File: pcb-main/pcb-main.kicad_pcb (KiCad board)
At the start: 2 copper layers, 86 x 86 mm, 37 parts, among them J1 AVR-ISP-6, J2 Conn_02x06_Counter_Clockwise, M1 Stepper_Motor, SW1 SW_MEC_5E, SW2 SW_MEC_5E, U1 ATmega328P-AU, U2 HT1621B-LQFP-A, U3 VIM878, U4 PCF8563T, Y1 16MHz, Y2 32kHz

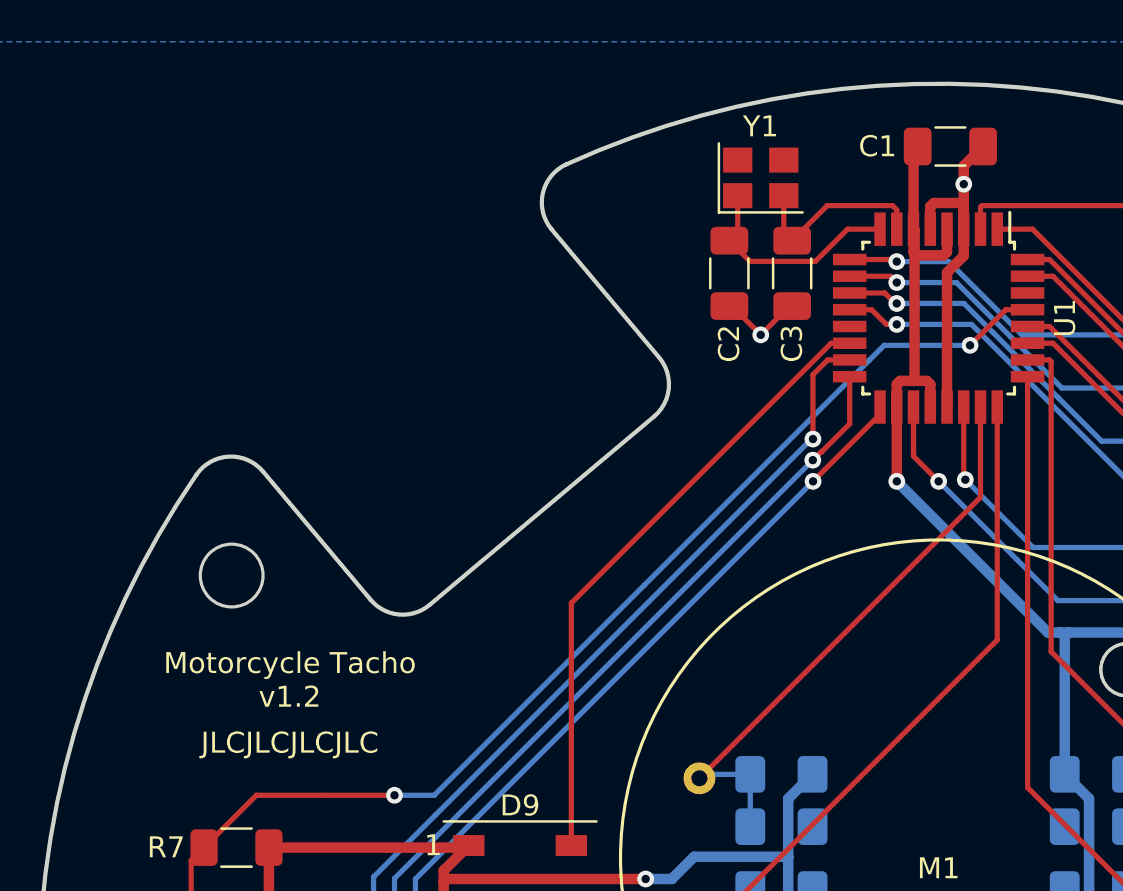
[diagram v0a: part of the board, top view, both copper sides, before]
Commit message: resolves #52: crystal circuit
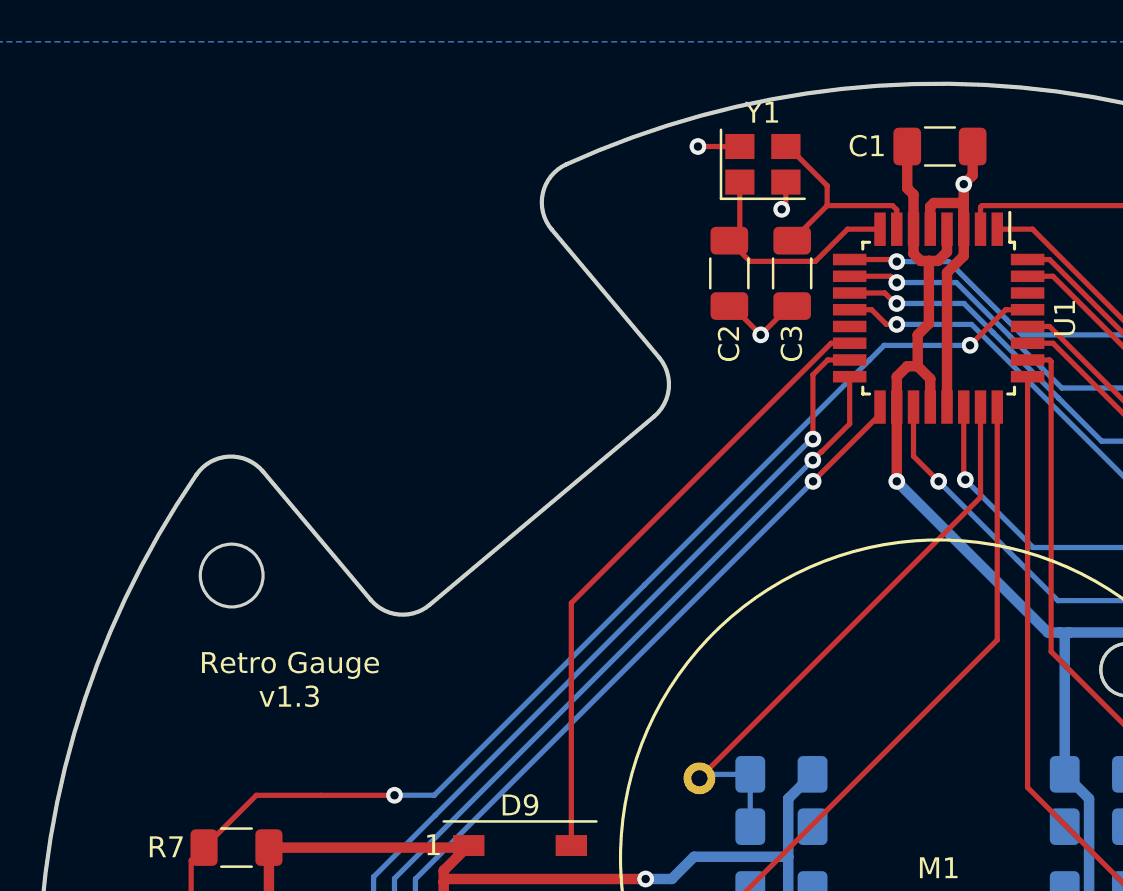
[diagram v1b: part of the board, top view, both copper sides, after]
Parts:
- R1: value 10k -> 100k
- Y1: value 16MHz -> Crystal_GND24
- moved Y1 0.66 mm to (141.6, 60.9)
- moved C1 0.50 mm to (150.1, 60.0)
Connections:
- Y1 pad 2: /XTAL1 -> GND
- Y1 pad 3: (no net) -> /XTAL1
- Y1 pad 4: (no net) -> GND
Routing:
- net GND: track 104.9 -> 108.0 mm, vias 10 -> 12
- net /XTAL1: track 9.02 -> 11.0 mm
- net +5V: track 263.5 -> 262.7 mm
- net /XTAL2: track 10.6 -> 11.3 mm
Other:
- board text added: "Retro Gauge v1.3"
- board text removed: "JLCJLCJLCJLC"
- board text removed: "Motorcycle Tacho v1.2"

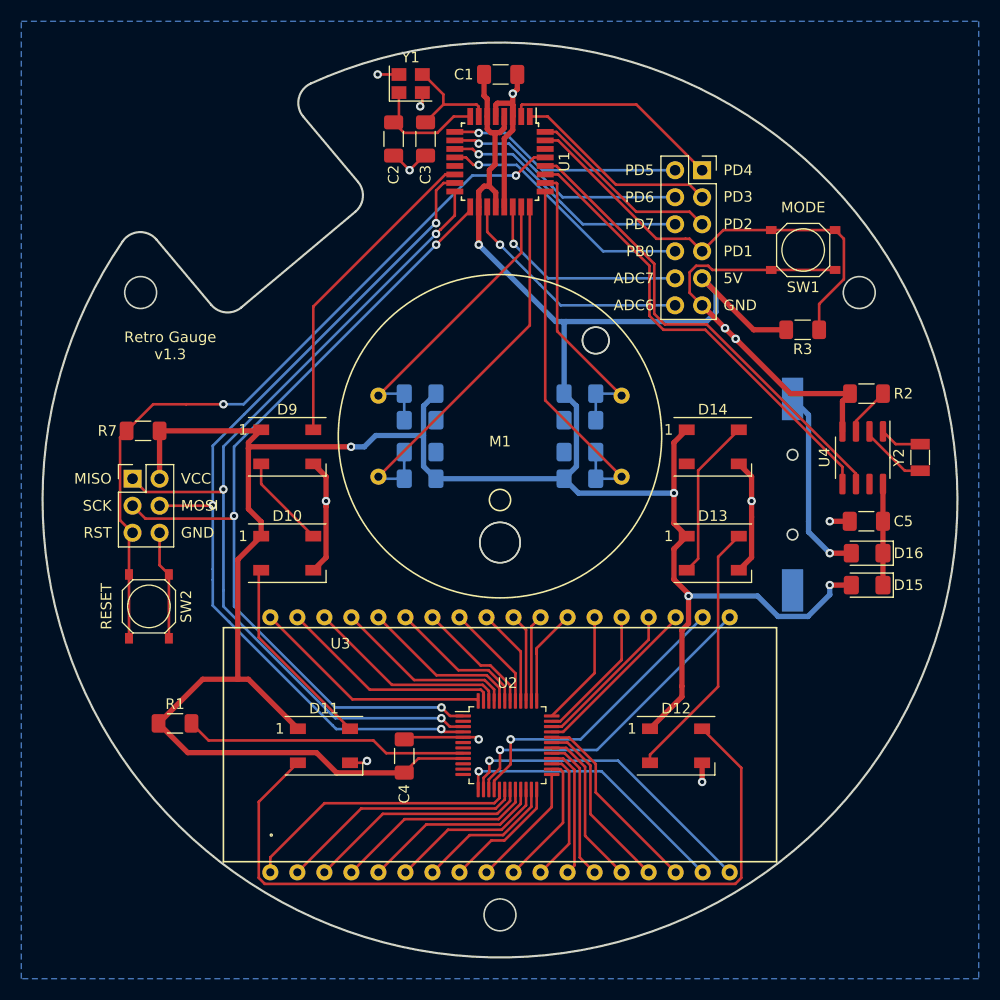
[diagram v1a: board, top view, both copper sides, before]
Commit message: resolves #48: neopixel caps
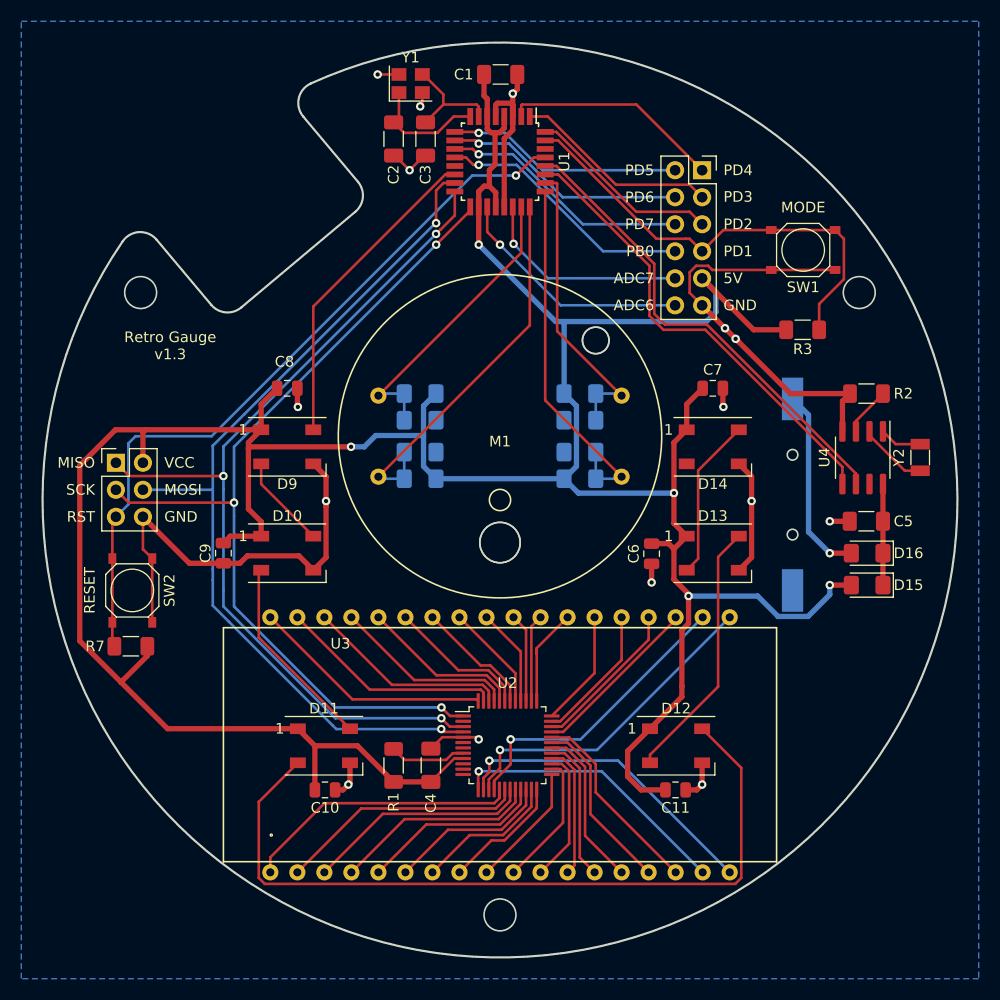
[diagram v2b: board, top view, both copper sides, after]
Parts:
- added C10: 100n, Capacitor_SMD:C_0805_2012Metric, F.Cu at (133.6, 127.2)
- added C11: 100n, Capacitor_SMD:C_0805_2012Metric, F.Cu at (166.5, 127.2)
- added C6: 100n, Capacitor_SMD:C_0805_2012Metric, F.Cu at (164.2, 105.0)
- added C7: 100n, Capacitor_SMD:C_0805_2012Metric, F.Cu at (170.0, 89.5)
- added C8: 100n, Capacitor_SMD:C_0805_2012Metric, F.Cu at (130.0, 89.5)
- added C9: 100n, Capacitor_SMD:C_0805_2012Metric, F.Cu at (124.0, 105.0)
- moved R1 20.9 mm to (140.0, 125.0), turned to 90 degrees
- moved R7 20.3 mm to (115.3, 113.8)
- moved C4 2.65 mm to (143.5, 124.9)
- moved J1 2.17 mm to (113.9, 96.5)
- moved SW2 2.17 mm to (115.4, 108.5)
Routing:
- net +5V: track 262.7 -> 300.1 mm
- net GND: track 108.0 -> 133.8 mm, vias 12 -> 15
- net Net-(R1-Pad2): track 26.7 -> 7.23 mm
- net /PB3: track 83.3 -> 84.8 mm, vias 3 -> 2
- net /PB4: track 84.4 -> 85.9 mm
- net /PB5: track 82.7 -> 84.2 mm
- net /XTAL1: track 11.0 -> 10.4 mm
- net /RESET: track 70.4 -> 70.1 mm, vias 2 -> 1

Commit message: pcb cleanup
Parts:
- moved R3 2.79 mm to (178.0, 81.2), turned to 0 degrees
- moved SW1 0.90 mm to (178.0, 75.8), turned to 90 degrees
- moved R7 0.20 mm to (115.5, 113.8)
- moved SW2 0.06 mm to (115.5, 108.5)
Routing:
- net GND: track 133.8 -> 119.2 mm, vias 15 -> 14
- net /PD1: track 43.1 -> 34.8 mm
- net /RESET: track 70.1 -> 66.8 mm
- net +5V: track 300.1 -> 297.9 mm, vias 5 -> 6

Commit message: update layout
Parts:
- removed SW2: SW_MEC_5E, footprints:TS_1187A
- added J3: Conn_01x02_Male, Connector_JST:JST_PH_S2B-PH-K_1x02_P2.00mm_Horizontal, F.Cu at (175.8, 77.8)
- C1, C2, C3, C4, C5: footprint Capacitor_SMD:C_1206_3216Metric_Pad1.33x1.80mm_HandSolder -> Capacitor_SMD:C_0805_2012Metric
- D15, D16: footprint Diode_SMD:D_1206_3216Metric_Pad1.42x1.75mm_HandSolder -> Diode_SMD:D_0805_2012Metric
- J2: footprint Connector_PinSocket_2.54mm:PinSocket_2x06_P2.54mm_Vertical -> Connector_PinHeader_2.00mm:PinHeader_2x06_P2.00mm_Vertical; moved to B.Cu
- R1, R2, R3, R7: footprint Resistor_SMD:R_1206_3216Metric_Pad1.30x1.75mm_HandSolder -> Resistor_SMD:R_0805_2012Metric
- SW1: value SW_MEC_5E -> SW_Push; footprint footprints:TS_1187A -> Button_Switch_SMD:SW_SPST_TL3342
- moved SW1 70.6 mm to (115.3, 108.3)
- moved J2 7.65 mm to (164.2, 63.0), turned to 180 degrees
- moved C5 7.34 mm to (189.0, 96.2), turned to 90 degrees
- moved Y2 6.95 mm to (186.0, 90.0), turned to 0 degrees
- moved C3 4.02 mm to (143.2, 62.0), turned to 90 degrees
- moved Y1 3.91 mm to (139.2, 63.9), turned to 90 degrees
- moved C2 3.25 mm to (143.2, 66.0)
- moved R3 2.98 mm to (179.8, 78.8), turned to 90 degrees
- moved R2 2.86 mm to (181.6, 90.0)
- moved D16 2.75 mm to (184.5, 102.2)
- moved BT1 2.75 mm to (177.5, 96.8), turned to 90 degrees
- moved D15 2.50 mm to (184.5, 105.5)
- moved D1 0.50 mm to (157.5, 89.5)
- moved D3 0.50 mm to (157.5, 98.5)
- moved D5 0.50 mm to (142.5, 89.5)
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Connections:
- R3 pad 1: /PD1 -> /PD0
- SW1 pad 1: /PD1 -> /RESET
- SW1 pad 2: /PD1 -> GND
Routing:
- net /PD0: track 0.00 -> 31.5 mm
- net /PD1: track 34.8 -> 11.2 mm
- net +5V: track 297.9 -> 311.2 mm
- net Net-(BT1-Pad1): track 18.0 -> 6.99 mm
- net GND: track 119.2 -> 109.1 mm, vias 14 -> 15
- net /PD2: track 18.3 -> 10.7 mm
- net /PD3: track 19.3 -> 11.9 mm
- net /PB0: track 24.4 -> 17.0 mm
- net /PD7: track 23.6 -> 16.9 mm
- net /ADC6: track 22.9 -> 16.3 mm
- net /PD4: track 20.6 -> 14.5 mm
- net /ADC7: track 20.0 -> 14.2 mm
- net /PD6: track 22.9 -> 17.2 mm
- net /PD5: track 22.2 -> 17.6 mm
- net /RESET: track 66.8 -> 70.5 mm
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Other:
- outline, holes or cut-outs redrawn

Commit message: update pcb layouts
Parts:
- M1: footprint footprints:Stepper Motor -> footprints:X27.168
- moved J2 0.25 mm to (164.0, 63.0)
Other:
- outline, holes or cut-outs redrawn

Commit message: v1.3 last minute changes
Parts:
- D15, D16: footprint Diode_SMD:D_0805_2012Metric -> Diode_SMD:D_SOD-323
- Y1: value Crystal_GND24 -> X322516MLB4SI
- Y2: value 32kHz -> Q13FC1350000400
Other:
- outline, holes or cut-outs redrawn
